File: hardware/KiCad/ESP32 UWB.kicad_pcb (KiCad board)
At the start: 2 copper layers, 72.3 x 32.6 mm, 56 parts, among them J1 HEADER-20P-2.54, J2 HEADER-12P-2.54, J3 10118194-0001LF, Q1 S8050, Q2 S8050, SW1 BUTTON, SW2 BUTTON, U1 AMS1117-3.3, U2 ESP32-C3-MINI-1-N4, U3 SILICON_LABS_CP2102N-A01-GQFN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

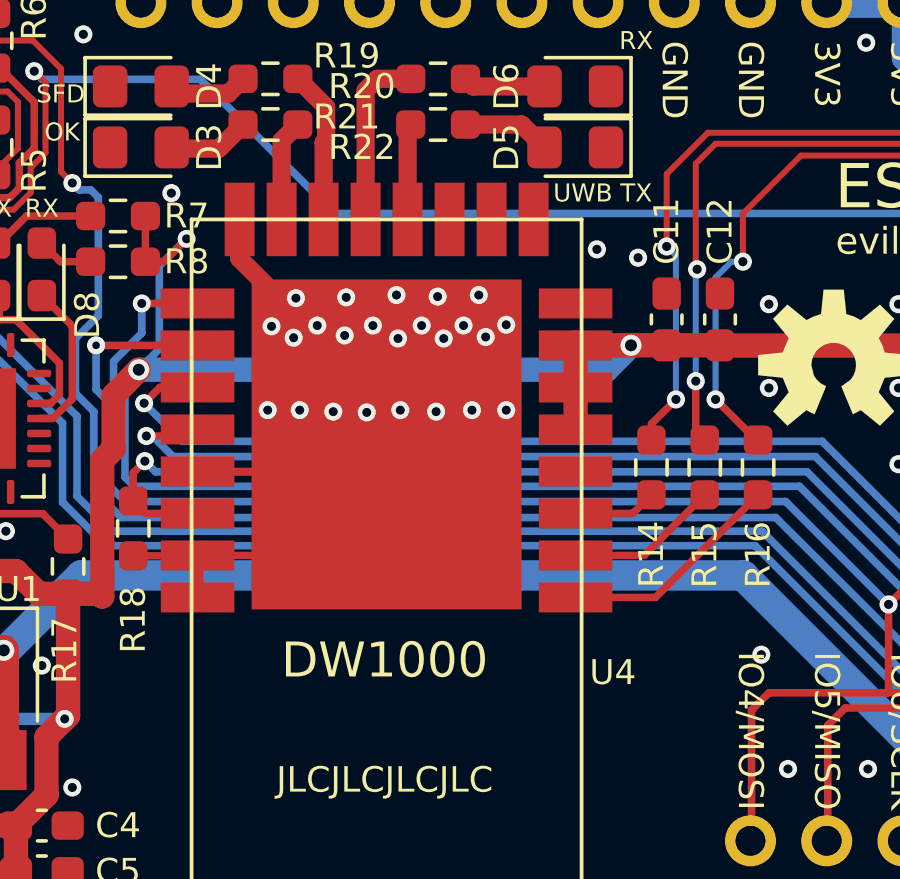
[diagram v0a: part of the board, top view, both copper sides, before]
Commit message: add BOM fields and tweak symbols and parts
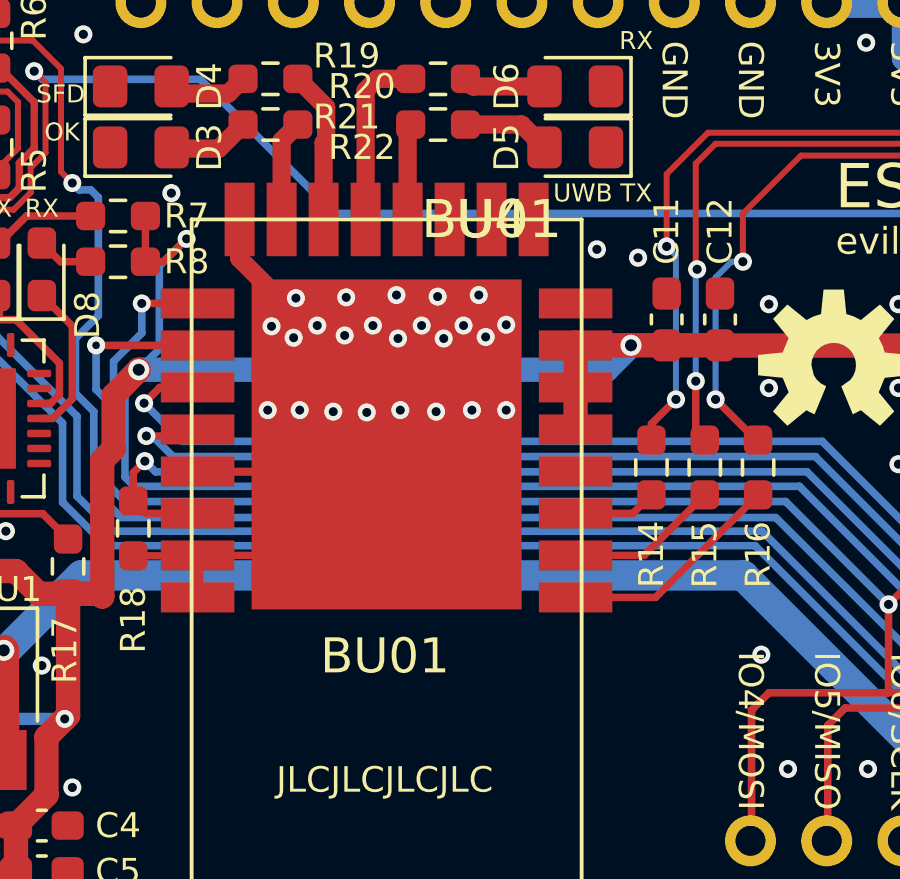
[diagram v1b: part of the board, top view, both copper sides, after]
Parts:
- C1, C12, C5, C7: value 10u -> 10uF/25V
- C11, C2, C4, C6, C8, C9: value 100n -> 100nF
- C3: value 10uF/16V -> 10uF/25V
- D2: value GREEN -> POWER (BLUE)
- D3: value GREEN -> UWB RXOK (YELLOW)
- D4: value GREEN -> UWB SFD (YELLOW)
- D5: value GREEN -> UWB TX (YELLOW)
- D6: value GREEN -> UWB RX (YELLOW)
- D7: value BLUE -> USB TX (RED)
- D8: value RED -> USB RX (RED)
- R10, R12, R9: value NC -> 10K
- R11, R13: value 10k -> 10K
- R17: value 1k -> 1K
- U4: value Val** -> BU01; footprint ESP32 UWB:DWM1000 -> ESP32 UWB:BU01
